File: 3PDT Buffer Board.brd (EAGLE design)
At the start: 37.8 x 21.6 mm, 17 parts, among them Q1 J201, SW2 3PDT

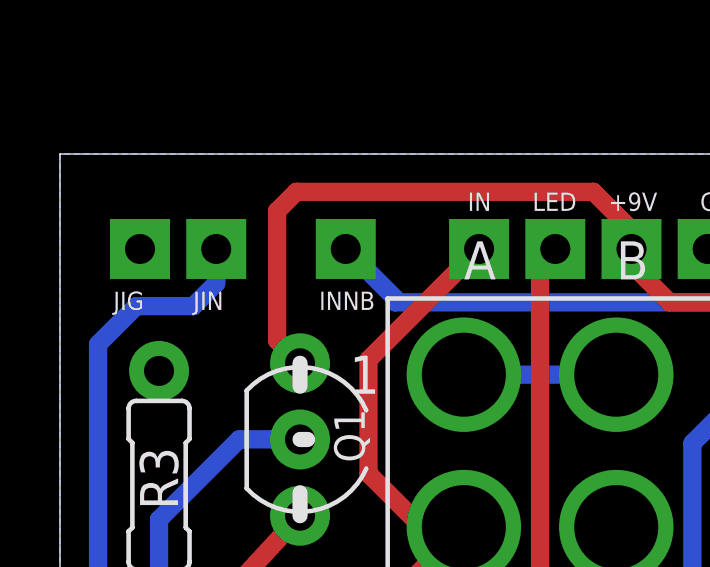
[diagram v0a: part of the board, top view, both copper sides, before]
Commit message: Made first panelized board
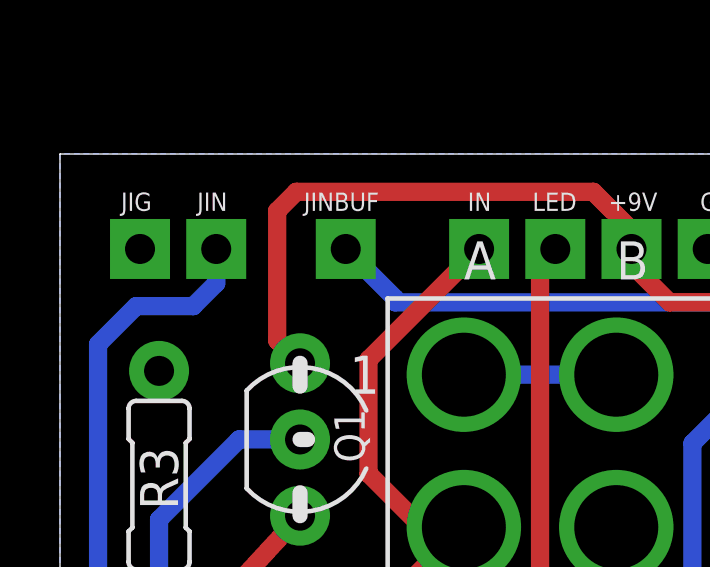
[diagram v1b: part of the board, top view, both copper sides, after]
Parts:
- renumbered INNB to JINBUF
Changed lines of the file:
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@@
 </element>
 <element name="JIG" library="mb_supply" package="SQUARE" value="GND(T)" x="2.667" y="18.415" smashed="yes">
-<attribute name="NAME" x="1.778" y="16.383" size="0.6096" layer="25" ratio="12"/>
+<attribute name="NAME" x="2.032" y="19.685" size="0.6096" layer="25" ratio="12"/>
 </element>
 <element name="JIN" library="mb_supply" package="SQUARE" value="" x="5.207" y="18.415" smashed="yes">
-<attribute name="NAME" x="4.445" y="16.383" size="0.6096" layer="25" ratio="12"/>
+<attribute name="NAME" x="4.572" y="19.685" size="0.6096" layer="25" ratio="12"/>
 </element>
 <element name="JOG" library="mb_supply" package="SQUARE" value="GND(T)" x="33.02" y="18.161" smashed="yes">
@@
 </element>
 <element name="SW2" library="mb_switches" package="3PDT" value="3PDT" x="18.542" y="9.144" smashed="yes"/>
-<element name="INNB" library="mb_supply" package="SQUARE" value="" x="9.525" y="18.415" smashed="yes">
-<attribute name="NAME" x="8.636" y="16.383" size="0.6096" layer="25" ratio="12"/>
+<element name="JINBUF" library="mb_supply" package="SQUARE" value="" x="9.525" y="18.415" smashed="yes">
+<attribute name="NAME" x="8.128" y="19.685" size="0.6096" layer="25" ratio="12"/>
 </element>
 </elements>
@@
 </signal>
 <signal name="N$6">
-<contactref element="INNB" pad="1"/>
+<contactref element="JINBUF" pad="1"/>
 <contactref element="C2" pad="1"/>
 <wire x1="28.702" y1="13.843" x2="25.908" y2="16.637" width="0.6096" layer="16"/>
